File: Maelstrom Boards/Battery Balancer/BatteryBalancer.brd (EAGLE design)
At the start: 101.7 x 101.6 mm, 34 parts, among them P1 39-30-14?

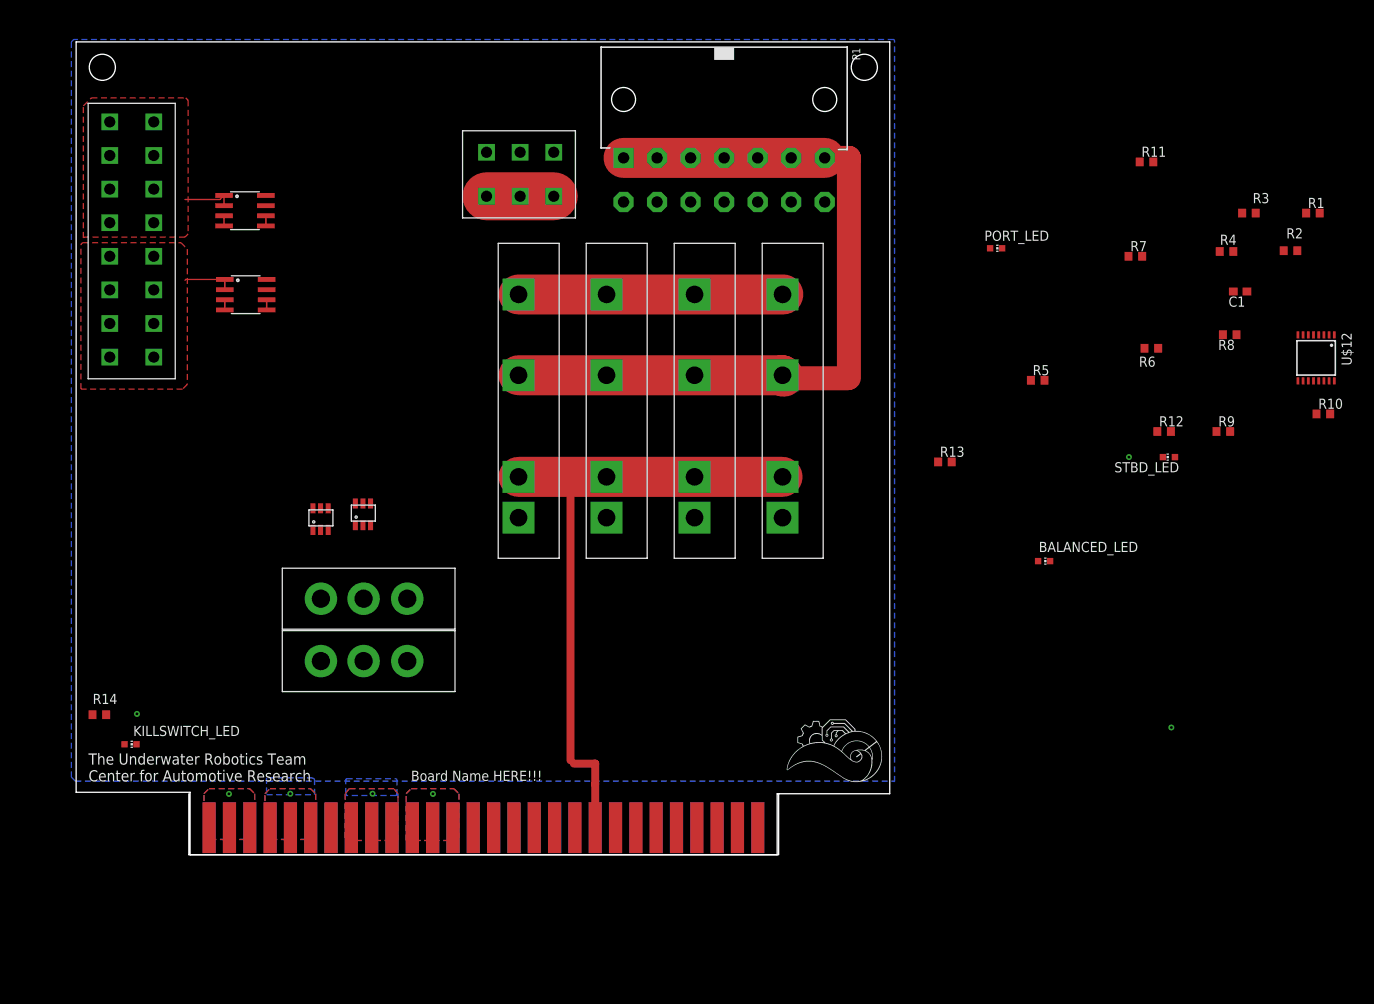
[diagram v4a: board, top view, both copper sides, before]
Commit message: Completed Battery Balancer
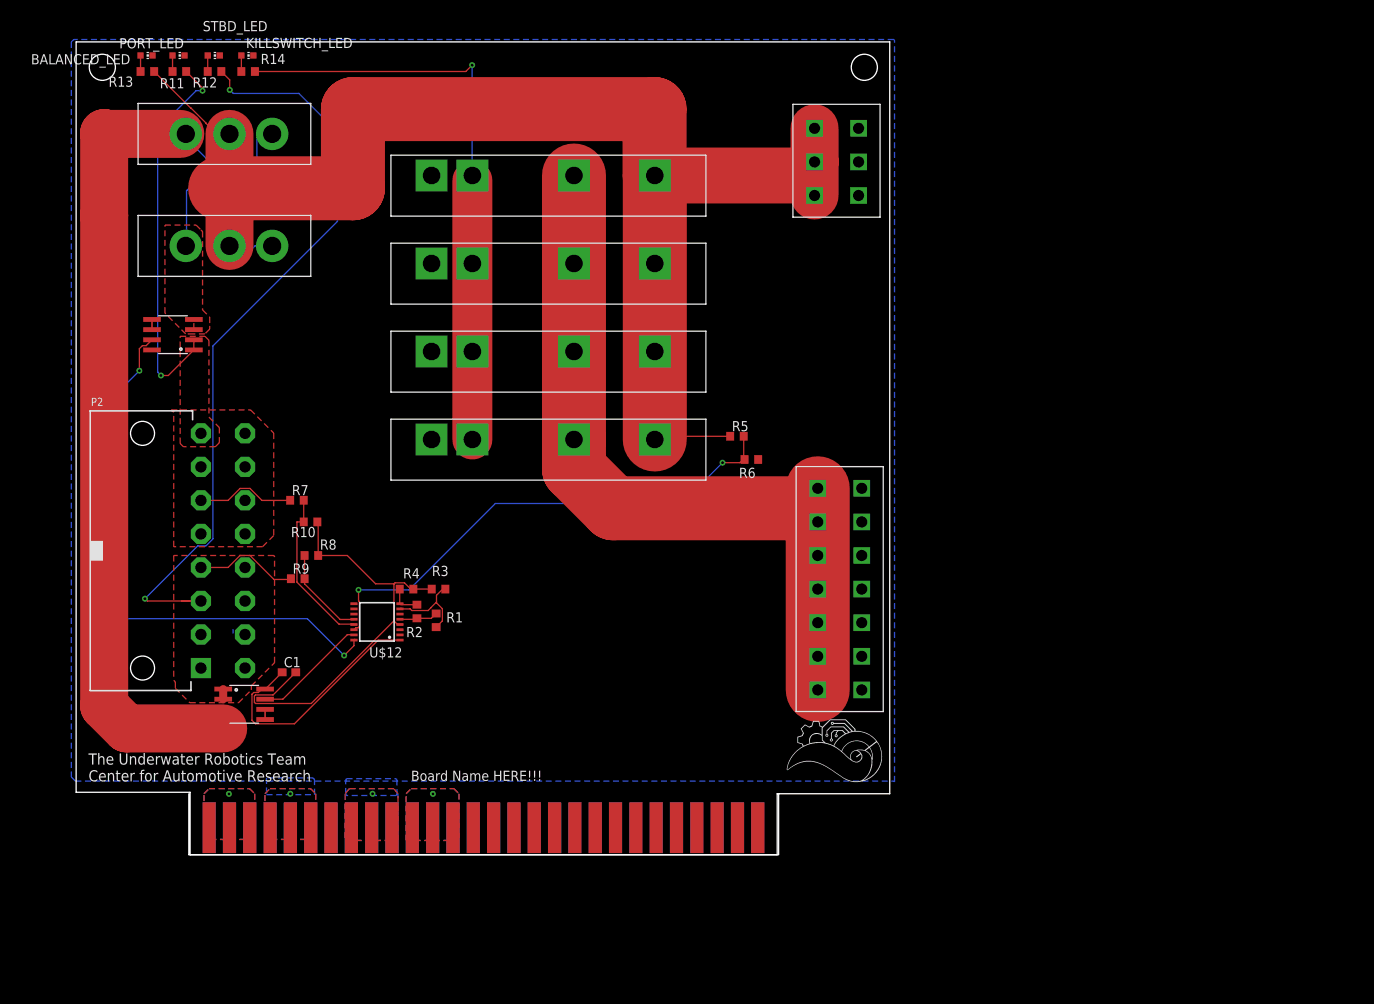
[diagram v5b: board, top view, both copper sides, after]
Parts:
- removed P1: 39-30-14?, con-molex-mini-fit:39-30-?14?
- removed U$14: 16PIN-VERT, Vertical_Connectors:16PIN_VERT
- added P2: 39-30-16?, con-molex-mini-fit:39-30-?16?
- added U$4: 14PIN-VERT, Vertical_Connectors:14PIN_VERT
- moved STBD_LED 129.5 mm to (17.1, 99.9), turned to 270 degrees
- moved BALANCED_LED 128.8 mm to (8.70, 99.9)
- moved C1 128.1 mm to (26.5, 22.8), turned to 0 degrees
- moved R10 127.3 mm to (29.2, 41.6), turned to 180 degrees
- moved R12 126.9 mm to (17.2, 97.9), turned to 180 degrees
- moved U$12 121.9 mm to (37.5, 29.1), turned to 180 degrees
- moved R11 121.4 mm to (12.8, 97.9), turned to 180 degrees
- moved R1 120.8 mm to (44.9, 29.3), turned to 270 degrees
- moved R2 118.1 mm to (42.5, 30.4), turned to 90 degrees
- moved R8 118.1 mm to (29.3, 37.4)
- moved R9 117.2 mm to (27.6, 34.5)
- moved R3 111.7 mm to (45.2, 33.2), turned to 180 degrees
- moved R13 111.0 mm to (8.80, 97.9)
- moved R4 110.8 mm to (41.2, 33.2)
- moved R7 109.1 mm to (27.5, 44.3)
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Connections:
- net GND: now also P2.10, P2.11, P2.12, P2.13, P2.14, P2.15, P2.16, P2.9, U$4.1-, U$4.2-, U$4.3-, U$4.4-, U$4.5-, U$4.6-, U$4.7-; no longer P1.10, P1.11, P1.12, P1.13, P1.14, P1.8, P1.9, U$14.1-, U$14.2-, U$14.3-, U$14.4-, U$14.5-, U$14.6-, U$14.7-, U$14.7-1
- net MOTOR_POWER: now also U$4.1+, U$4.2+, U$4.3+, U$4.4+, U$4.5+, U$4.6+, U$4.7+; no longer P1.1, P1.2, P1.3, P1.4, P1.5, P1.6, P1.7
- net PORT_BATTERY: now also P2.5, P2.6, P2.7, P2.8; no longer U$14.5+, U$14.6+, U$14.7+, U$14.7+1
- net STBD_BATTERY: now also P2.1, P2.2, P2.3, P2.4; no longer U$14.1+, U$14.2+, U$14.3+, U$14.4+
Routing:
- net BALANCED_OUT: track 41.6 -> 189.5 mm
- net N$4: track 1.27 -> 113.3 mm
- net STBD_BATTERY: track 6.30 -> 111.6 mm, vias 0 -> 2
- net PORT_CURRENT: track 0.00 -> 68.6 mm, vias 0 -> 2
- net N$15: track 0.00 -> 63.4 mm, vias 0 -> 2
- net GNDA: track 0.00 -> 54.8 mm
- net PORT_BATTERY: track 6.36 -> 61.1 mm, vias 0 -> 2
- net +3V3: track 0.00 -> 31.3 mm
- net N$9: track 0.00 -> 20.4 mm
- net N$2: track 0.00 -> 20.0 mm
- net STBD_CURRENT: track 0.00 -> 14.5 mm
- net N$5: track 0.00 -> 13.1 mm
- net N$10: track 0.00 -> 11.6 mm
- net N$7: track 0.00 -> 11.3 mm
- net N$1: track 1.27 -> 10.00 mm
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- added copper zone on layer 1, net N$1

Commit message: Fixed and updated Battery Balancer
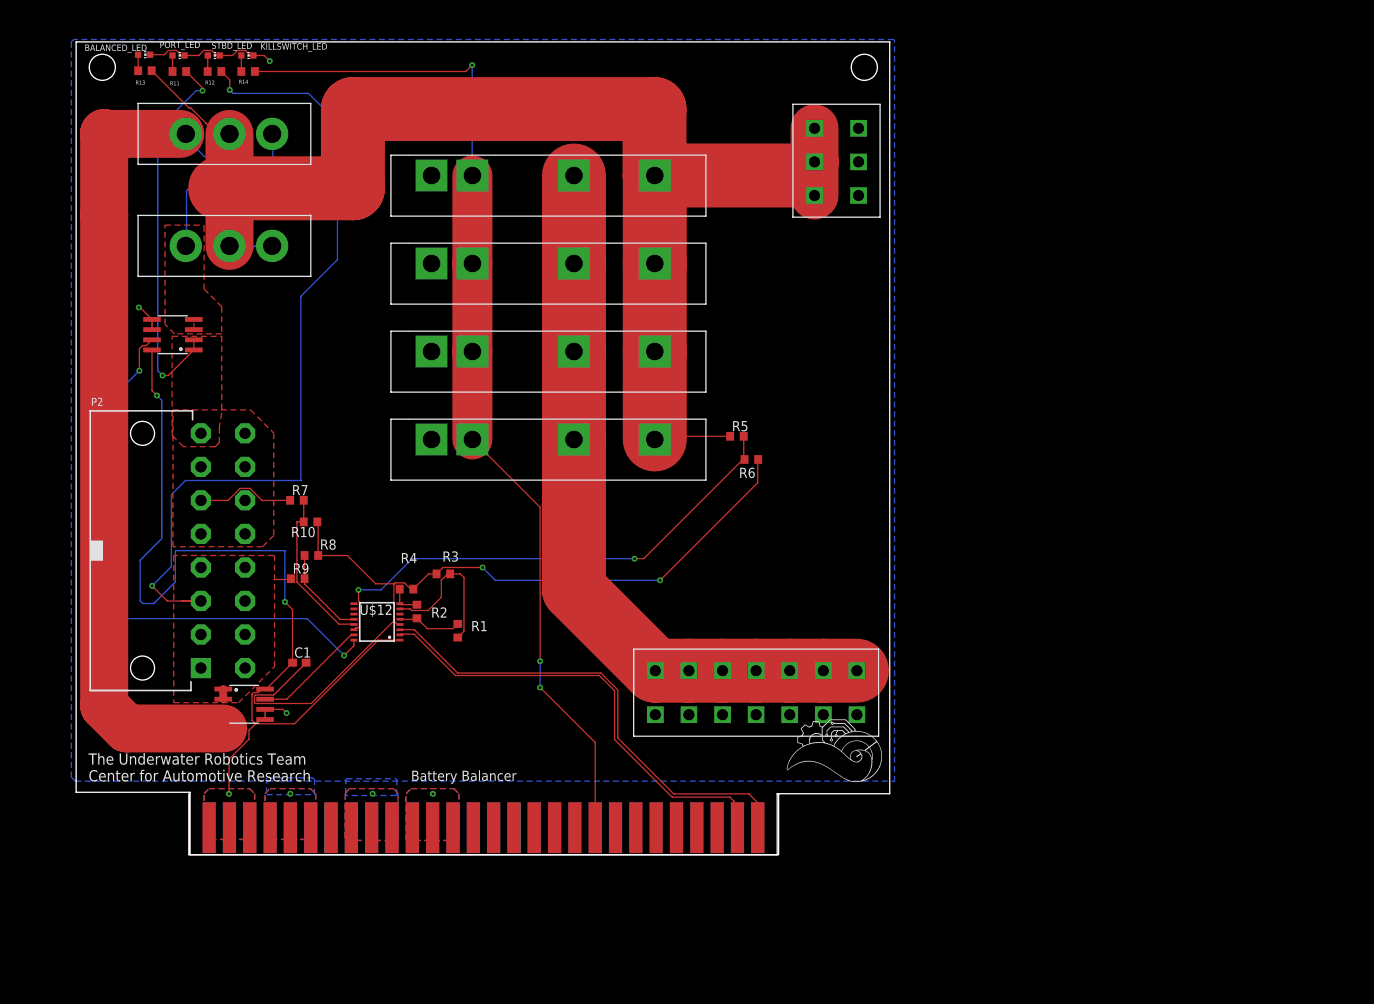
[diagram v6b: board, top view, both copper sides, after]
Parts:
- moved U$4 20.4 mm to (72.3, 23.0), turned to 270 degrees
- moved R1 3.00 mm to (47.6, 28.0)
- moved R3 1.99 mm to (45.8, 35.1)
- moved C1 1.77 mm to (27.8, 24.0)
- moved R13 0.32 mm to (8.50, 98.0)
- moved BALANCED_LED 0.32 mm to (8.40, 100.0)
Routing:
- net +3V3: track 31.3 -> 113.9 mm, vias 1 -> 3
- net SENSOR_SCL: track 0.00 -> 59.2 mm
- net SENSOR_SDA: track 0.30 -> 57.8 mm
- net KILL_SWITCH: track 74.1 -> 129.6 mm, vias 1 -> 3
- net GNDA: track 54.8 -> 107.1 mm, vias 0 -> 2
- net GND: track 2.91 -> 24.8 mm, vias 2 -> 5
- net N$7: track 11.3 -> 19.4 mm
- net STBD_BATTERY: track 111.6 -> 106.6 mm
- net MOTOR_POWER: track 95.4 -> 91.3 mm
- net N$8: track 4.83 -> 8.06 mm
- net BALANCED_OUT: track 189.5 -> 187.6 mm
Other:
- board text added: "Battery Balancer"
- board text removed: "Board Name HERE!!!"

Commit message: Finalized and updated Battery Balancer Board
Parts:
- moved U$13 55.7 mm to (91.6, 26.7)
- moved R6 20.3 mm to (74.8, 31.5)
- moved R5 18.6 mm to (73.2, 36.2)
- moved U$10 7.50 mm to (58.1, 44.4)
- moved U$11 7.50 mm to (58.1, 55.4)
- moved U$8 7.50 mm to (58.1, 66.4)
- moved U$9 7.50 mm to (58.1, 77.4)
- moved R2 6.88 mm to (47.7, 25.9)
- moved R1 6.44 mm to (52.1, 23.4)
- moved R3 6.44 mm to (50.3, 30.5)
- moved U$12 6.44 mm to (42.0, 24.5)
- moved R4 6.15 mm to (45.6, 28.9)
- moved R8 5.69 mm to (34.2, 34.5)
- moved U$2 5.60 mm to (17.2, 76.3)
- moved U$15 5.60 mm to (17.8, 70.5)
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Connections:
- net N$4 renamed SOURCE
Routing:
- net N$2: track 20.0 -> 40.5 mm, vias 0 -> 2
- net N$15: track 63.4 -> 47.9 mm
- net BALANCED_OUT: track 187.6 -> 202.1 mm, vias 0 -> 1
- net SOURCE: track 113.6 -> 100.0 mm
- net GNDA: track 107.1 -> 94.2 mm
- net N$9: track 20.4 -> 29.4 mm
- net SENSOR_SDA: track 57.8 -> 49.8 mm
- net N$10: track 11.6 -> 19.6 mm
- net SENSOR_SCL: track 59.2 -> 52.5 mm
- net KILL_SWITCH: track 129.6 -> 123.4 mm
- net STBD_BATTERY: track 106.6 -> 101.6 mm
- net PORT_CURRENT: track 68.6 -> 72.1 mm
- net +3V3: track 113.9 -> 117.3 mm
- net MOTOR_POWER: track 91.3 -> 88.6 mm
- net N$1: track 9.97 -> 12.7 mm, vias 0 -> 1
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- added copper zone on layer 1, net SOURCE

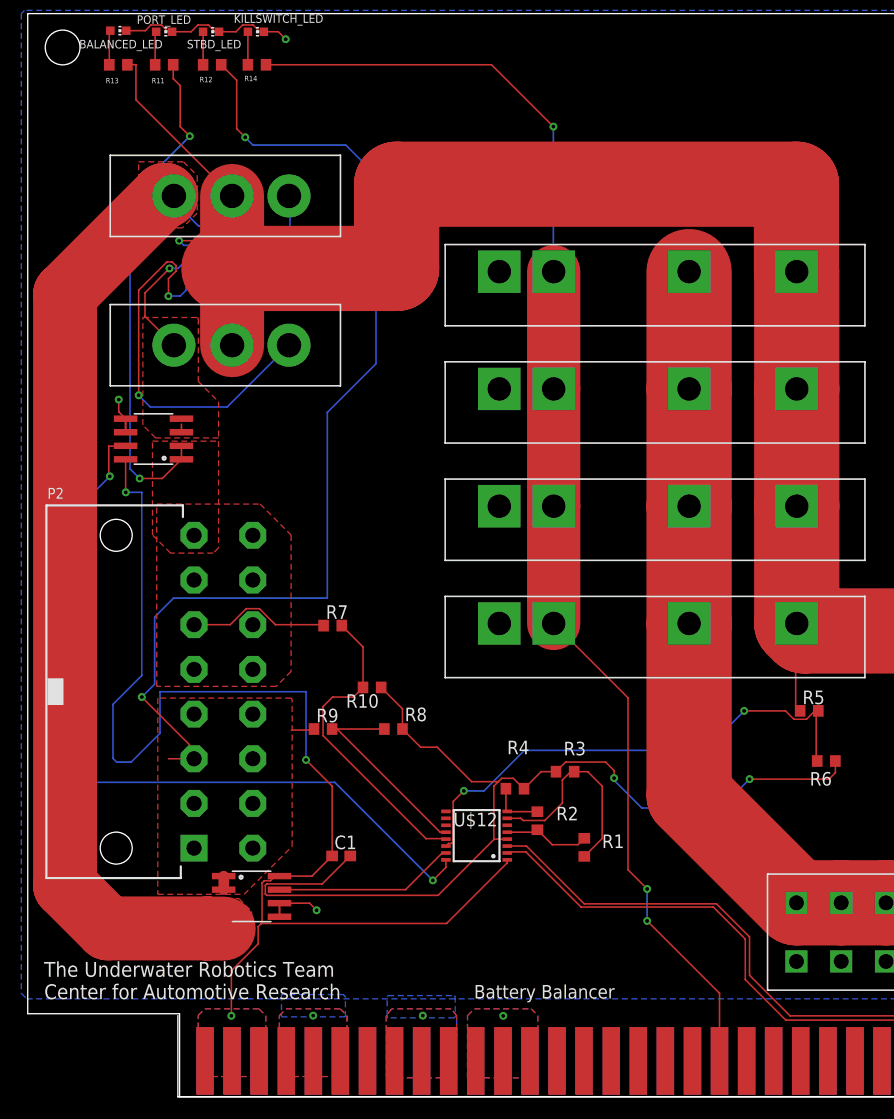
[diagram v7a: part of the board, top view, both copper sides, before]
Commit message: Finalized the battery balancer
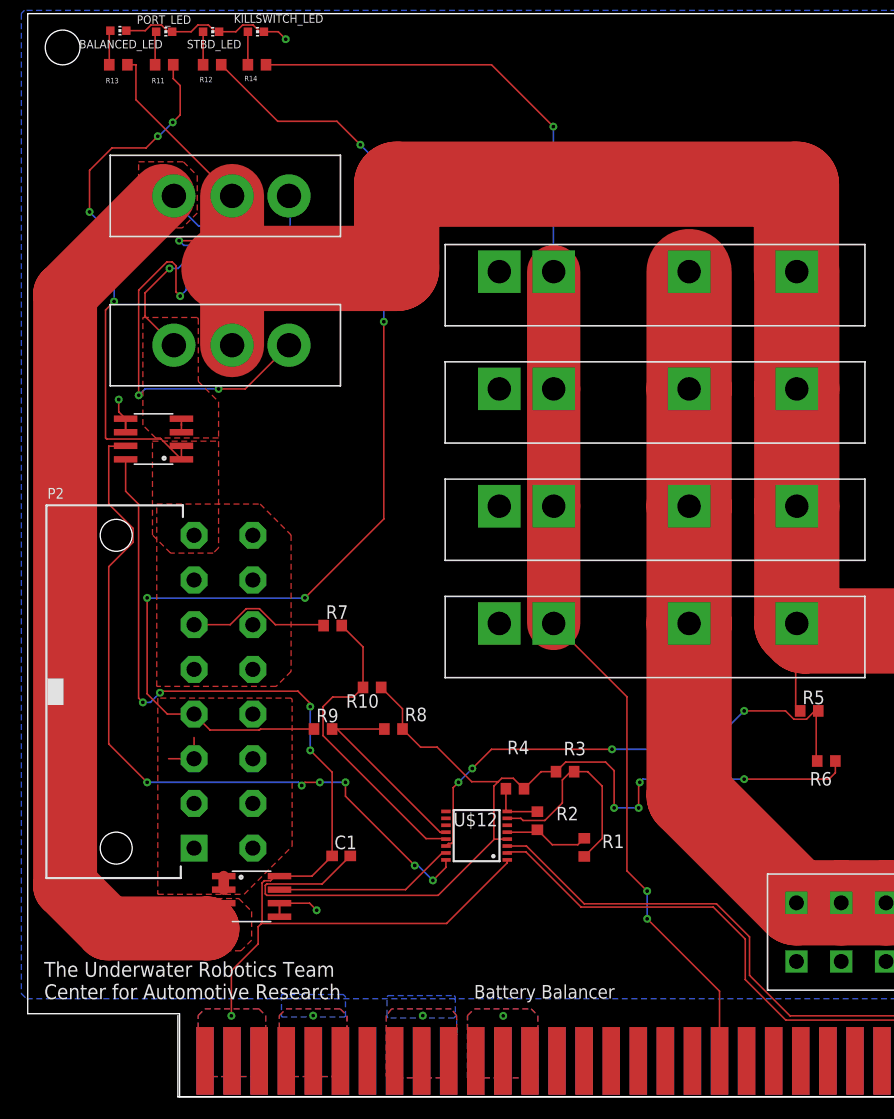
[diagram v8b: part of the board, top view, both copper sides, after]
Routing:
- net +3V3: track 117.3 -> 102.2 mm, vias 3 -> 5
- net STBD_BATTERY: track 101.6 -> 109.2 mm, vias 2 -> 4
- net PORT_BATTERY: track 61.6 -> 64.7 mm, vias 2 -> 4
- net GNDA: track 94.2 -> 97.0 mm, vias 2 -> 4
- net N$2: track 40.5 -> 38.4 mm, vias 2 -> 3
- net PORT_CURRENT: track 72.1 -> 70.6 mm, vias 2 -> 6
- net SOURCE: track 100.0 -> 99.0 mm
- net N$15: track 47.9 -> 48.7 mm, vias 2 -> 4
- net N$1: track 12.7 -> 13.2 mm
